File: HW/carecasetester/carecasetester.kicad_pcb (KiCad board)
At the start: 2 copper layers, 158.3 x 161.1 mm, 84 parts, among them J1 Conn_01x16_Female, J10-TP22 Conn_01x01_Male, J11-TP7 Conn_01x01_Male, J12-TP14 Conn_01x01_Male, J13-TP23 Conn_01x01_Male, J14-TP17 Conn_01x01_Male, J15 Conn_01x16_Male, J15-TP1 Conn_01x01_Male, J15-TP20 Conn_01x01_Male, J16-TP2 Conn_01x01_Male, J16-TP24 Conn_01x01_Male, J17-TP3 Conn_01x01_Male, J18-TP4 Conn_01x01_Male, J19-TP6 Conn_01x01_Male, J2 Conn_01x16_Female, J20-TP9 Conn_01x01_Male, J21-TP10 Conn_01x01_Male, J22-TP11 Conn_01x01_Male, J23-TP12 Conn_01x01_Male, J24-TP15 Conn_01x01_Male, J25-TP18 Conn_01x01_Male, J26-TP5 Conn_01x01_Male, J27-TP26 Conn_01x01_Male, J28-TP25 Conn_01x01_Male, J3 Conn_01x04_Female, J4 Conn_01x06_Male, J4-TP16 Conn_01x01_Male, J5 12V_Psu, J5-TP8 Conn_01x01_Male, J5-~E1 Conn_01x02_Male, J6-TP21 Conn_01x01_Male, J7-TP27 Conn_01x01_Male, J8-TP13 Conn_01x01_Male, J9-TP19 Conn_01x01_Male, K1 AZ952, K2 AZ952, Q1 BC847W, Q2 BC847W, SW1 SW_DIP_x02, U1 CD74HC4067M, U2 L7805

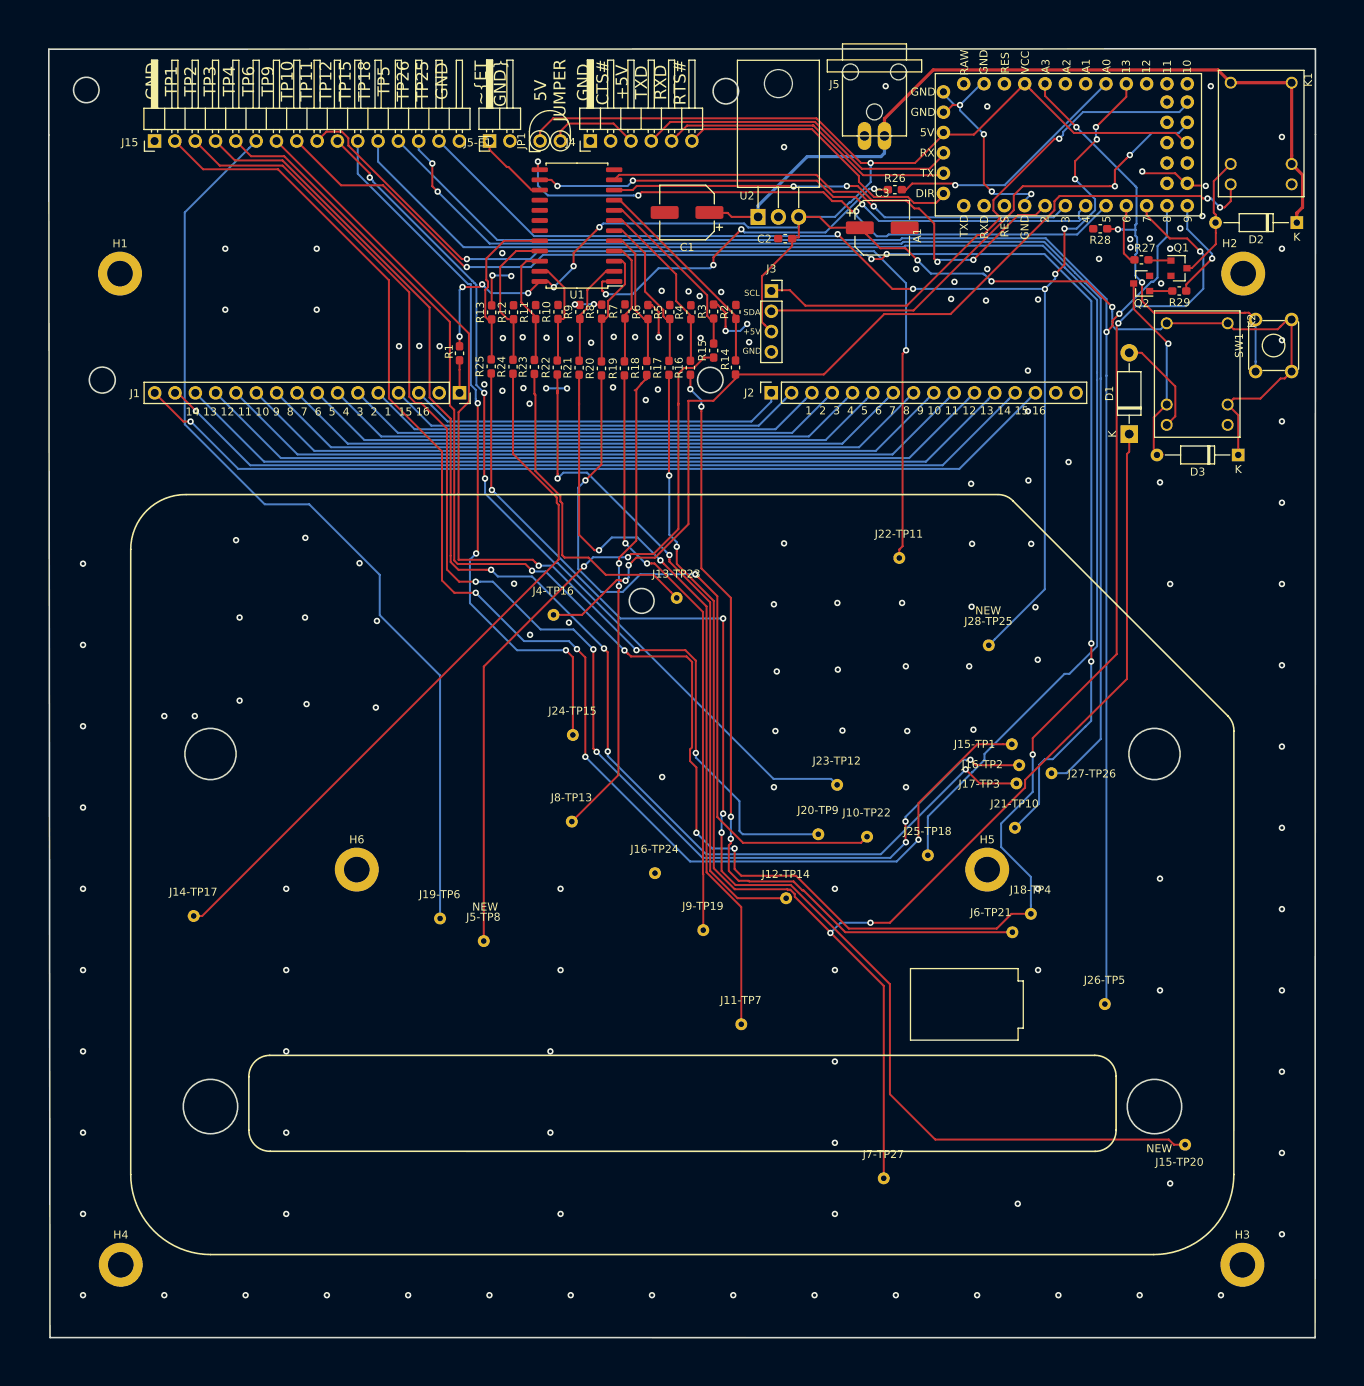
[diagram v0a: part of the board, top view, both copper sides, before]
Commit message: pcb updated for new rev. ready to plot gerbers
footprints saved for later use

software fixed PCF8574A1 now works with new setup and with in house displays
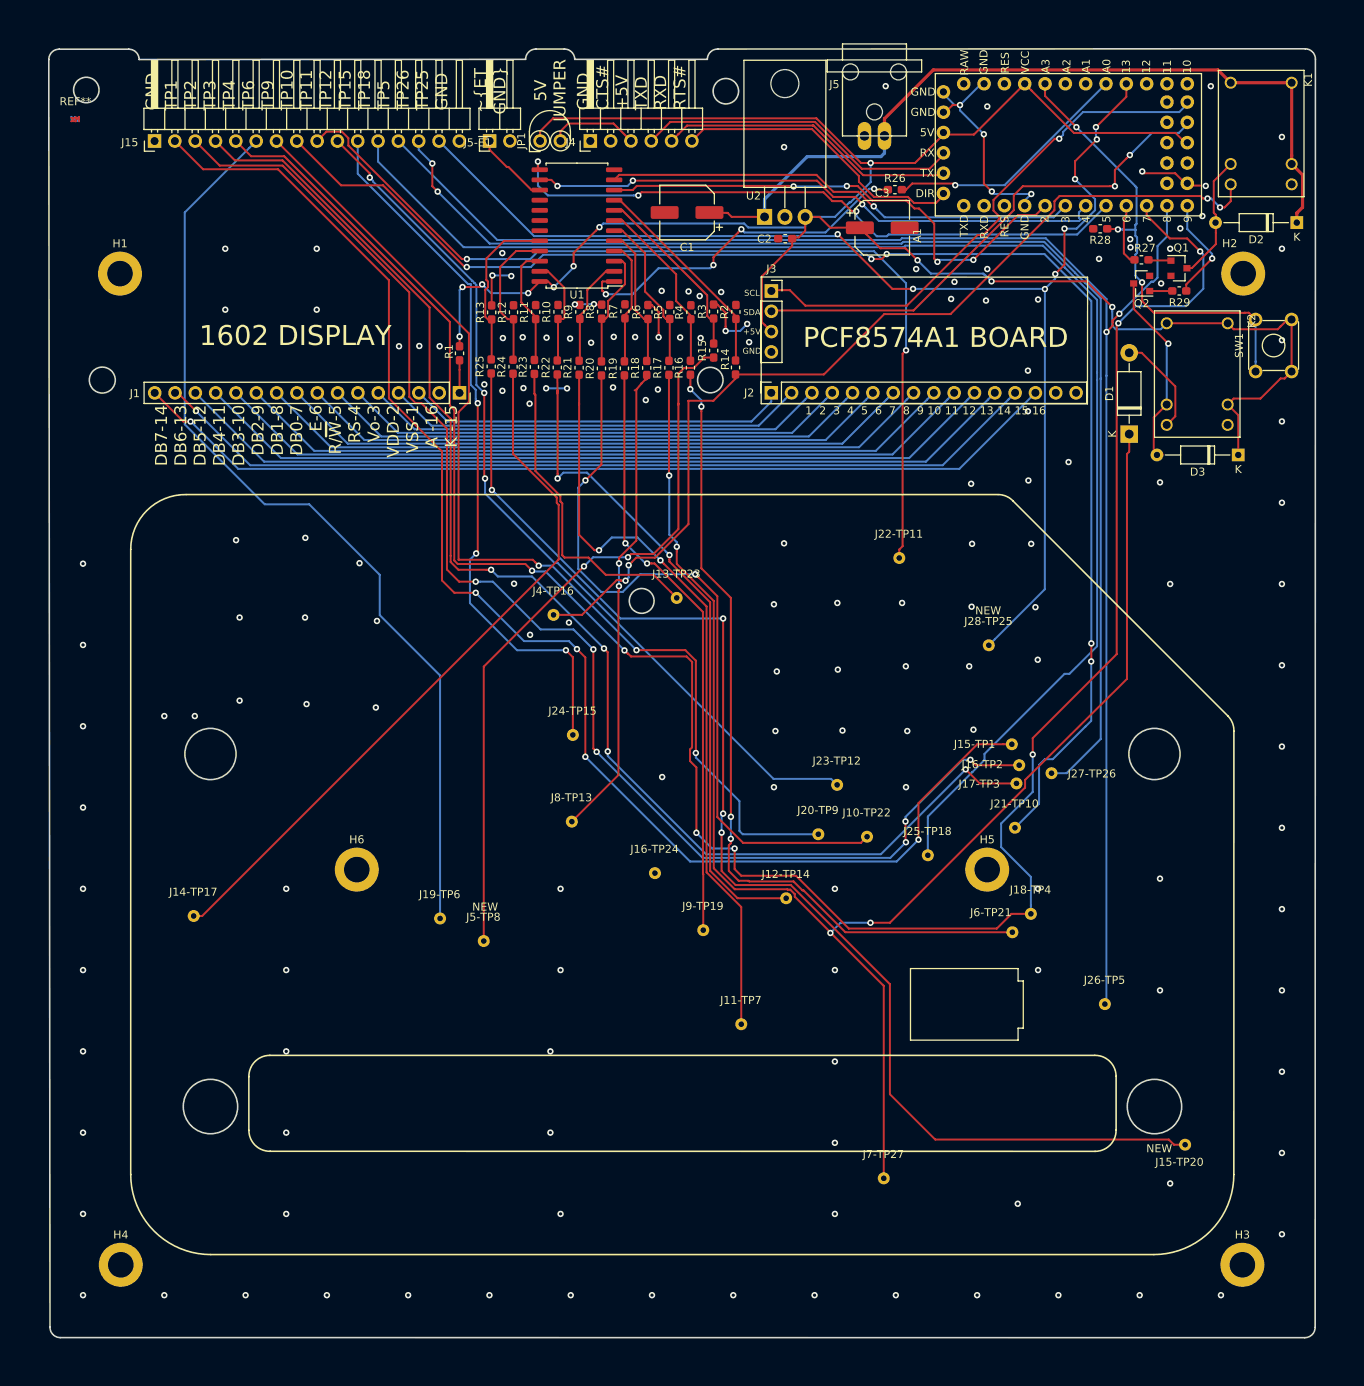
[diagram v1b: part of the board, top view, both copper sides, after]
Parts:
- added REF**: MM-COPPERMARK, MM:MM-COPPERMARK, F.Cu at (80.3, 17.9)
- added REF**: MM-COPPERMARK, MM:MM-COPPERMARK, B.Cu at (80.3, 17.9)
- moved U2 0.81 mm to (166.5, 30.3)
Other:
- outline, holes or cut-outs redrawn
- board text added: "1602 DISPLAY"
- board text added: "DB7-14 DB6-13 DB5-12 DB4-11 DB3-10 DB2-9 DB1-8 DB0-7 E-6 R/~W~-5 RS-4 Vo-3 VDD-2 VSS-1 A -16 K -15"
- board text added: "DCTMM_CC-TESTER V0.22 07/08/2020"
- board text added: "PCF8574A1 BOARD"
- board text removed: "14 13 12 11 10 9 8 7 6 5 4 3 2 1 15 16"
- board text removed: "DCTMM_CC-TESTER V0.22 03/08/2020"
- board text removed: "Flip display headder"
- board text removed: "GND TP1 TP2 TP3 TP4 TP6 TP9 TP10 TP11 TP12 TP15 TP18 TP5 TP26 GND GND"

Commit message: dfgdfg
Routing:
- net Net-(J15-Pad14): track 159.0 -> 157.9 mm
- net Net-(J15-Pad8): track 179.8 -> 179.2 mm
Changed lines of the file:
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@@
     (thickness 1)
     (drawings 156)
-    (tracks 1314)
+    (tracks 1310)
     (zones 0)
     (modules 86)
@@
   (segment (start 183.83002 33.43) (end 183.61001 33.65001) (width 0.25) (layer B.Cu) (net 29))
   (segment (start 205.29 37.3) (end 205.29 37.29) (width 0.25) (layer B.Cu) (net 29))
-  (segment (start 204.21999 99.85) (end 208.49 95.57999) (width 0.25) (layer B.Cu) (net 29))
-  (segment (start 202.34 99.85) (end 204.21999 99.85) (width 0.25) (layer B.Cu) (net 29))
   (segment (start 208.49 40.49) (end 206.550001 38.550001) (width 0.25) (layer B.Cu) (net 29))
   (segment (start 208.49 40.49) (end 208.49 50.58) (width 0.25) (layer B.Cu) (net 29))
-  (segment (start 208.49 95.57999) (end 208.49 50.58) (width 0.25) (layer B.Cu) (net 29))
   (segment (start 208.49 50.58) (end 208.49 50.49) (width 0.25) (layer B.Cu) (net 29))
+  (segment (start 208.49 93.59) (end 208.49 50.58) (width 0.25) (layer B.Cu) (net 29))
+  (segment (start 202.34 99.85) (end 202.34 99.74) (width 0.25) (layer B.Cu) (net 29))
+  (segment (start 202.34 99.74) (end 208.49 93.59) (width 0.25) (layer B.Cu) (net 29))
   (via (at 141.64 84.48) (size 0.8) (drill 0.4) (layers F.Cu B.Cu) (net 30))
   (segment (start 141.64 84.48) (end 142.52 85.36) (width 0.25) (layer F.Cu) (net 30))
@@
   (segment (start 207.31499 83.626846) (end 207.31499 85.86501) (width 0.25) (layer F.Cu) (net 33))
   (segment (start 207.31499 85.86501) (end 207.3 85.88) (width 0.25) (layer F.Cu) (net 33))
-  (segment (start 200.78 98.82) (end 200.78 103.66) (width 0.25) (layer B.Cu) (net 33))
-  (segment (start 201.5 98.1) (end 200.78 98.82) (width 0.25) (layer B.Cu) (net 33))
-  (segment (start 200.78 103.66) (end 197.77 106.67) (width 0.25) (layer B.Cu) (net 33))
-  (segment (start 207.3 85.88) (end 207.3 93.31) (width 0.25) (layer B.Cu) (net 33))
-  (segment (start 207.3 93.31) (end 206.62 93.99) (width 0.25) (layer B.Cu) (net 33))
-  (segment (start 206.608998 93.99) (end 202.498998 98.1) (width 0.25) (layer B.Cu) (net 33))
-  (segment (start 202.498998 98.1) (end 201.5 98.1) (width 0.25) (layer B.Cu) (net 33))
-  (segment (start 206.62 93.99) (end 206.608998 93.99) (width 0.25) (layer B.Cu) (net 33))
   (segment (start 201.04 34.96) (end 181.74 34.96) (width 0.25) (layer B.Cu) (net 33))
   (segment (start 201.46 34.96) (end 201.04 34.96) (width 0.25) (layer B.Cu) (net 33))
@@
   (segment (start 181.12 35.58) (end 181.74 34.96) (width 0.25) (layer F.Cu) (net 33))
   (segment (start 137.260064 36.579936) (end 138.79 35.05) (width 0.25) (layer B.Cu) (net 33))
+  (segment (start 200.78 98.82) (end 200.78 103.66) (width 0.25) (layer B.Cu) (net 33))
+  (segment (start 200.78 103.66) (end 197.77 106.67) (width 0.25) (layer B.Cu) (net 33))
+  (segment (start 207.3 85.88) (end 207.3 92.3) (width 0.25) (layer B.Cu) (net 33))
+  (segment (start 207.3 92.3) (end 200.78 98.82) (width 0.25) (layer B.Cu) (net 33))
   (via (at 150.46 84.47) (size 0.8) (drill 0.4) (layers F.Cu B.Cu) (net 34))
   (segment (start 150.46 84.47) (end 156.57 84.47) (width 0.25) (layer F.Cu) (net 34))
@@
   (via (at 199.99 97.51) (size 0.8) (drill 0.4) (layers F.Cu B.Cu) (net 67))
   (segment (start 199.99 95.463002) (end 199.99 97.51) (width 0.25) (layer F.Cu) (net 67))
-  (segment (start 199.99 97.51) (end 199.99 102.19) (width 0.25) (layer B.Cu) (net 67))
-  (segment (start 199.99 102.19) (end 196.04 106.14) (width 0.25) (layer B.Cu) (net 67))
-  (segment (start 199.76 116.36934) (end 199.76 117.43) (width 0.25) (layer B.Cu) (net 67))
-  (segment (start 199.76 112.808998) (end 199.76 116.36934) (width 0.25) (layer B.Cu) (net 67))
-  (segment (start 196.04 109.088998) (end 199.76 112.808998) (width 0.25) (layer B.Cu) (net 67))
-  (segment (start 196.04 106.14) (end 196.04 109.088998) (width 0.25) (layer B.Cu) (net 67))
   (segment (start 197.34 117.43) (end 199.76 117.43) (width 0.25) (layer F.Cu) (net 67))
   (segment (start 195.5 119.27) (end 197.34 117.43) (width 0.25) (layer F.Cu) (net 67))
+  (segment (start 199.76 116.36934) (end 199.76 117.43) (width 0.25) (layer B.Cu) (net 67))
+  (segment (start 199.99 97.51) (end 199.99 102.19) (width 0.25) (layer B.Cu) (net 67))
+  (segment (start 196.04 106.14) (end 196.04 107.96) (width 0.25) (layer B.Cu) (net 67))
+  (segment (start 199.99 102.19) (end 196.04 106.14) (width 0.25) (layer B.Cu) (net 67))
+  (segment (start 196.04 107.96) (end 199.76 111.68) (width 0.25) (layer B.Cu) (net 67))
+  (segment (start 199.76 111.68) (end 199.76 116.36934) (width 0.25) (layer B.Cu) (net 67))
   (segment (start 140.95 19.617919) (end 141.927919 18.64) (width 0.25) (layer F.Cu) (net 68))
   (segment (start 140.95 20.82) (end 140.95 19.617919) (width 0.25) (layer F.Cu) (net 68))

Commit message: gerbers and drill files made
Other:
- board text added: "DCTMM_CC-TESTER V0.23 07/08/2020"
- board text removed: "DCTMM_CC-TESTER V0.22 07/08/2020"
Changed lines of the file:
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@@
       (usegerberextensions true)
       (usegerberattributes false)
-      (usegerberadvancedattributes false)
+      (usegerberadvancedattributes true)
       (creategerberjobfile false)
       (excludeedgelayer false)
@@
       (viasonmask false)
       (mode 1)
-      (useauxorigin true)
+      (useauxorigin false)
       (hpglpennumber 1)
       (hpglpenspeed 20)
@@
       (drillshape 0)
       (scaleselection 1)
-      (outputdirectory "gerber/V02/"))
+      (outputdirectory "gerber/V023/"))
   )
   (net 0 "")
@@
   )
   (gr_line (start 195.64 65.02) (end 94.18 65.02) (layer F.SilkS) (width 0.2))
-  (gr_text "DCTMM_CC-TESTER V0.22\n07/08/2020" (at 157.44 153.44) (layer B.SilkS)
+  (gr_text "DCTMM_CC-TESTER V0.23\n07/08/2020" (at 157.44 153.44) (layer B.SilkS)
     (effects (font (size 1.5 1.5) (thickness 0.3)) (justify mirror))
   )
@@
   )
   (dimension 161.160005 (width 0.15) (layer Dwgs.User)
-    (gr_text "161,160 mm" (at 240.28 89.881231 89.98577916) (layer Dwgs.User)
+    (gr_text "161,160 mm" (at 240.27 89.871231 89.98577916) (layer Dwgs.User)
       (effects (font (size 1 1) (thickness 0.15)))
     )
-    (feature1 (pts (xy 235.3 170.46) (xy 239.546421 170.461054)))
-    (feature2 (pts (xy 235.34 9.3) (xy 239.586421 9.301054)))
-    (crossbar (pts (xy 239 9.300908) (xy 238.96 170.460908)))
-    (arrow1a (pts (xy 238.96 170.460908) (xy 238.373859 169.334259)))
-    (arrow1b (pts (xy 238.96 170.460908) (xy 239.5467 169.33455)))
-    (arrow2a (pts (xy 239 9.300908) (xy 238.4133 10.427266)))
-    (arrow2b (pts (xy 239 9.300908) (xy 239.586141 10.427557)))
+    (feature1 (pts (xy 235.29 170.45) (xy 239.536421 170.451054)))
+    (feature2 (pts (xy 235.33 9.29) (xy 239.576421 9.291054)))
+    (crossbar (pts (xy 238.99 9.290908) (xy 238.95 170.450908)))
+    (arrow1a (pts (xy 238.95 170.450908) (xy 238.363859 169.324259)))
+    (arrow1b (pts (xy 238.95 170.450908) (xy 239.5367 169.32455)))
+    (arrow2a (pts (xy 238.99 9.290908) (xy 238.4033 10.417266)))
+    (arrow2b (pts (xy 238.99 9.290908) (xy 239.576141 10.417557)))
   )
   (dimension 158.26 (width 0.15) (layer Dwgs.User)
